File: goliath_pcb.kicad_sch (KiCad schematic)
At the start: 58 parts, among them IC1 MCT9001SD, IC2 MCT9001SD, IC3 MCT9001SD, IC4 MCT9001SD, IC5 MCT9001SD, IC6 MCT9001SD, IC7 MCT9001SD, J1 RJ45_LED, J2 RJ45_LED, J3 RJ45_LED, J4 RJ45_LED, J5 Conn_01x10, U1 Pico, U2 LM7805_TO220, U3 74HCT244, U4 74HCT244, U5 LTC1298CS8-PBF

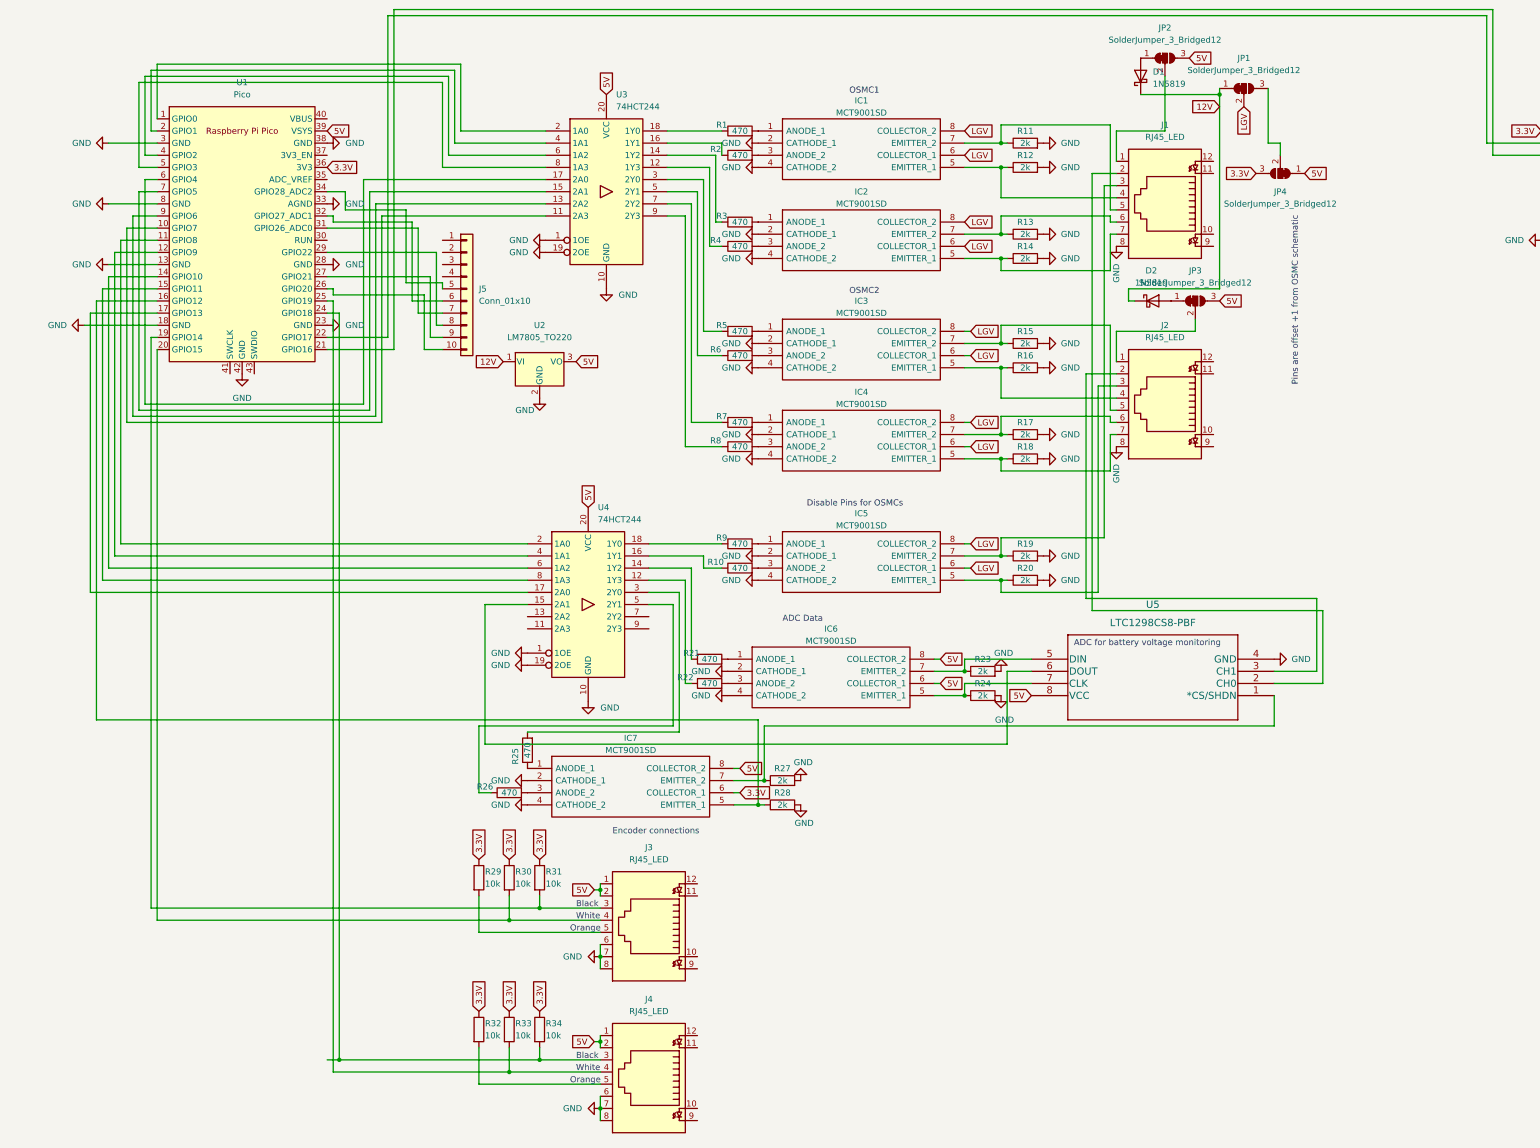
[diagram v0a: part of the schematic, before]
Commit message: Add extra I/O and extra headers, expand PCB
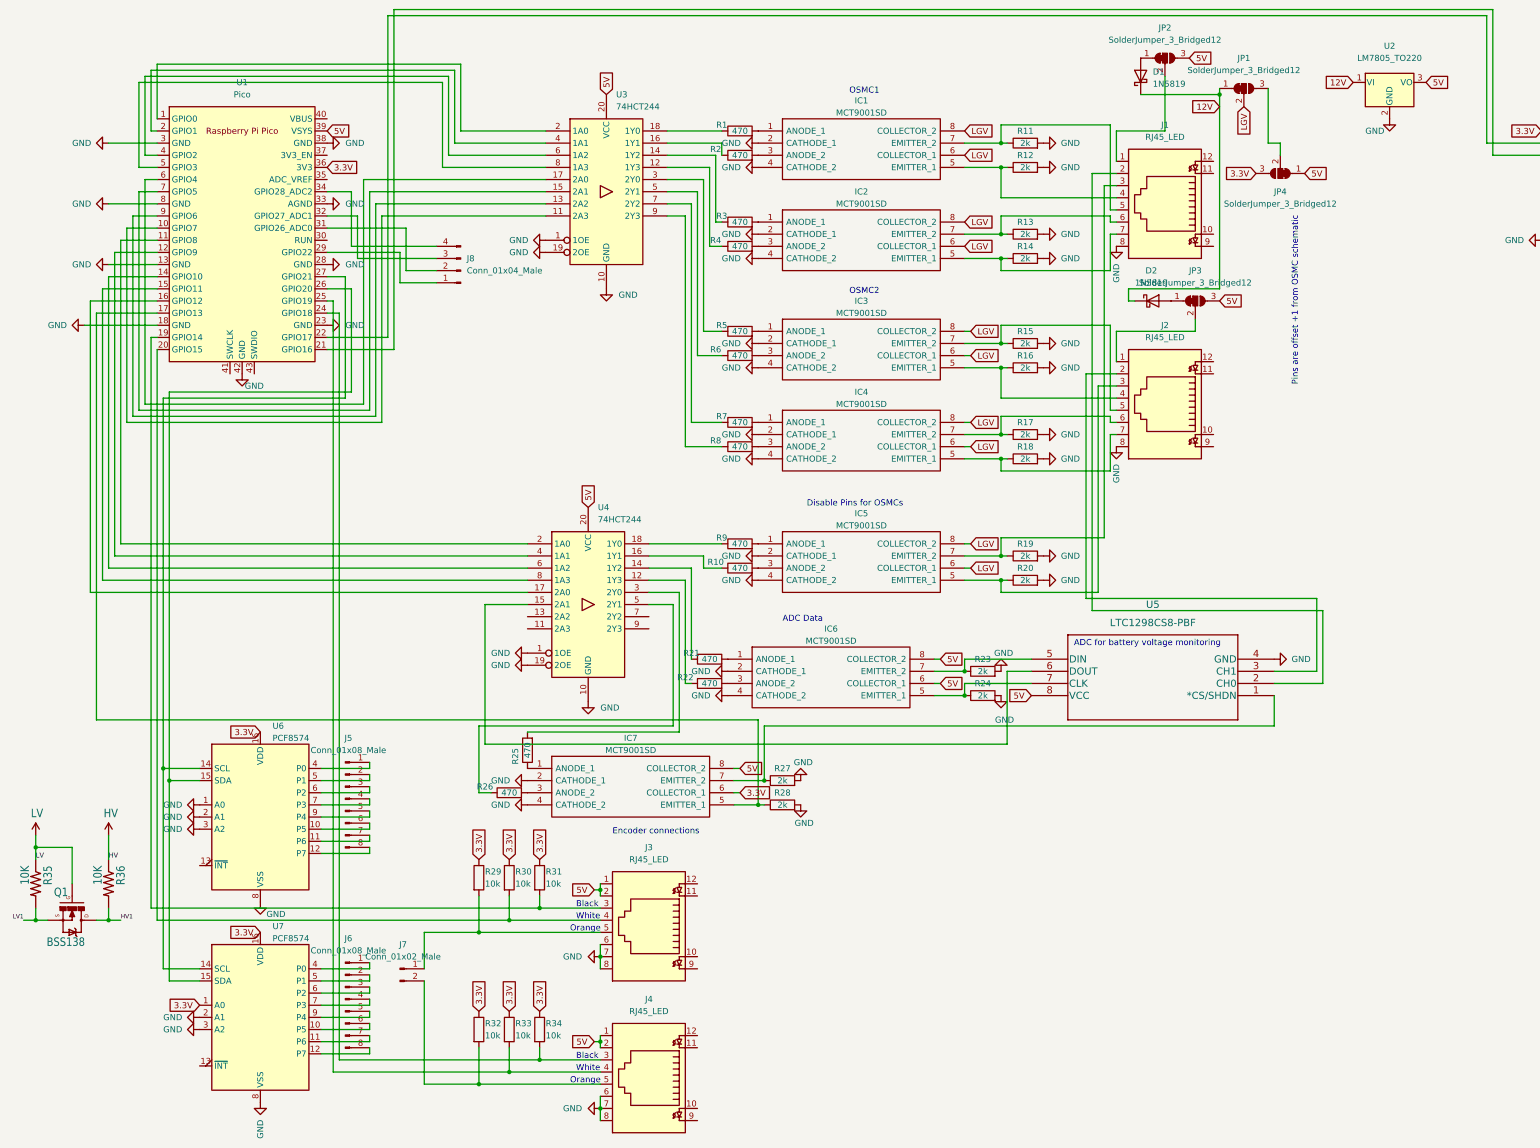
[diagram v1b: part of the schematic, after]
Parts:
- removed J5: Conn_01x10, symbol Connector_Generic:Conn_01x10
- added J5, J6: Conn_01x08_Male, Connector_PinHeader_2.54mm:PinHeader_1x08_P2.54mm_Vertical, symbol Connector:Conn_01x08_Male
- added J7: Conn_01x02_Male, Connector_PinHeader_2.54mm:PinHeader_1x02_P2.54mm_Vertical, symbol Connector:Conn_01x02_Male
- added J8: Conn_01x04_Male, Connector_PinHeader_2.54mm:PinHeader_1x04_P2.54mm_Vertical, symbol Connector:Conn_01x04_Male
- added Q1: BSS138, goliath_pcb:SOT23-3, symbol goliath_pcb-eagle-import:MOSFET-NCHANNELSMD
- added R35, R36: 10K, goliath_pcb:0603-RES, symbol goliath_pcb-eagle-import:RESISTOR0603-RES
- added U6, U7: PCF8574, Package_DIP:DIP-16_W7.62mm_Socket, symbol Interface_Expansion:PCF8574
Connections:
- net 3.3V: now also U6.16 (VDD), U7.1 (A0), U7.16 (VDD)
- net GND: now also U6.1 (A0), U6.2 (A1), U6.3 (A2), U6.8 (VSS), U7.2 (A1), U7.3 (A2), U7.8 (VSS)
- net at J3.5, R29.2: now also J7.1 (Pin_1)
- net at J4.5, R32.2: now also J7.2 (Pin_2)
- net at U4.17 (2A0): now also U1.16 (GPIO12); no longer U1.17 (GPIO13)
- net at IC7.5 (EMITTER_1), R28.1: now also U1.17 (GPIO13); no longer U1.16 (GPIO12)
- net at U1.26 (GPIO20): now also U6.15 (SDA), U7.15 (SDA)
- net at U1.27 (GPIO21): now also U6.14 (SCL), U7.14 (SCL)
- net at U1.29 (GPIO22): now also J8.1 (Pin_1)
- net at U1.31 (GPIO26_ADC0): now also J8.2 (Pin_2)
- net at U1.32 (GPIO27_ADC1): now also J8.3 (Pin_3)
- net at U1.34 (GPIO28_ADC2): now also J8.4 (Pin_4)
- new net: J6.6 (Pin_6), U7.10 (P5)
- new net: J6.7 (Pin_7), U7.11 (P6)
- new net: J6.8 (Pin_8), U7.12 (P7)
- new net: J6.1 (Pin_1), U7.4 (P0)
- new net: J6.2 (Pin_2), U7.5 (P1)
- new net: J6.3 (Pin_3), U7.6 (P2)
- new net: J6.4 (Pin_4), U7.7 (P3)
- new net: J6.5 (Pin_5), U7.9 (P4)
- new net: J5.1 (Pin_1), U6.4 (P0)
- new net: J5.2 (Pin_2), U6.5 (P1)
- new net: J5.3 (Pin_3), U6.6 (P2)
- new net: J5.4 (Pin_4), U6.7 (P3)
- new net: J5.5 (Pin_5), U6.9 (P4)
- new net: J5.6 (Pin_6), U6.10 (P5)
- new net: J5.7 (Pin_7), U6.11 (P6)
- new net: J5.8 (Pin_8), U6.12 (P7)
- new net HV1: Q1.3 (D), R36.2
- new net LV1: Q1.2 (S), R35.2
- new net VCC: Q1.1 (G), R35.1, R36.1
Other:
- moved on the sheet: U2

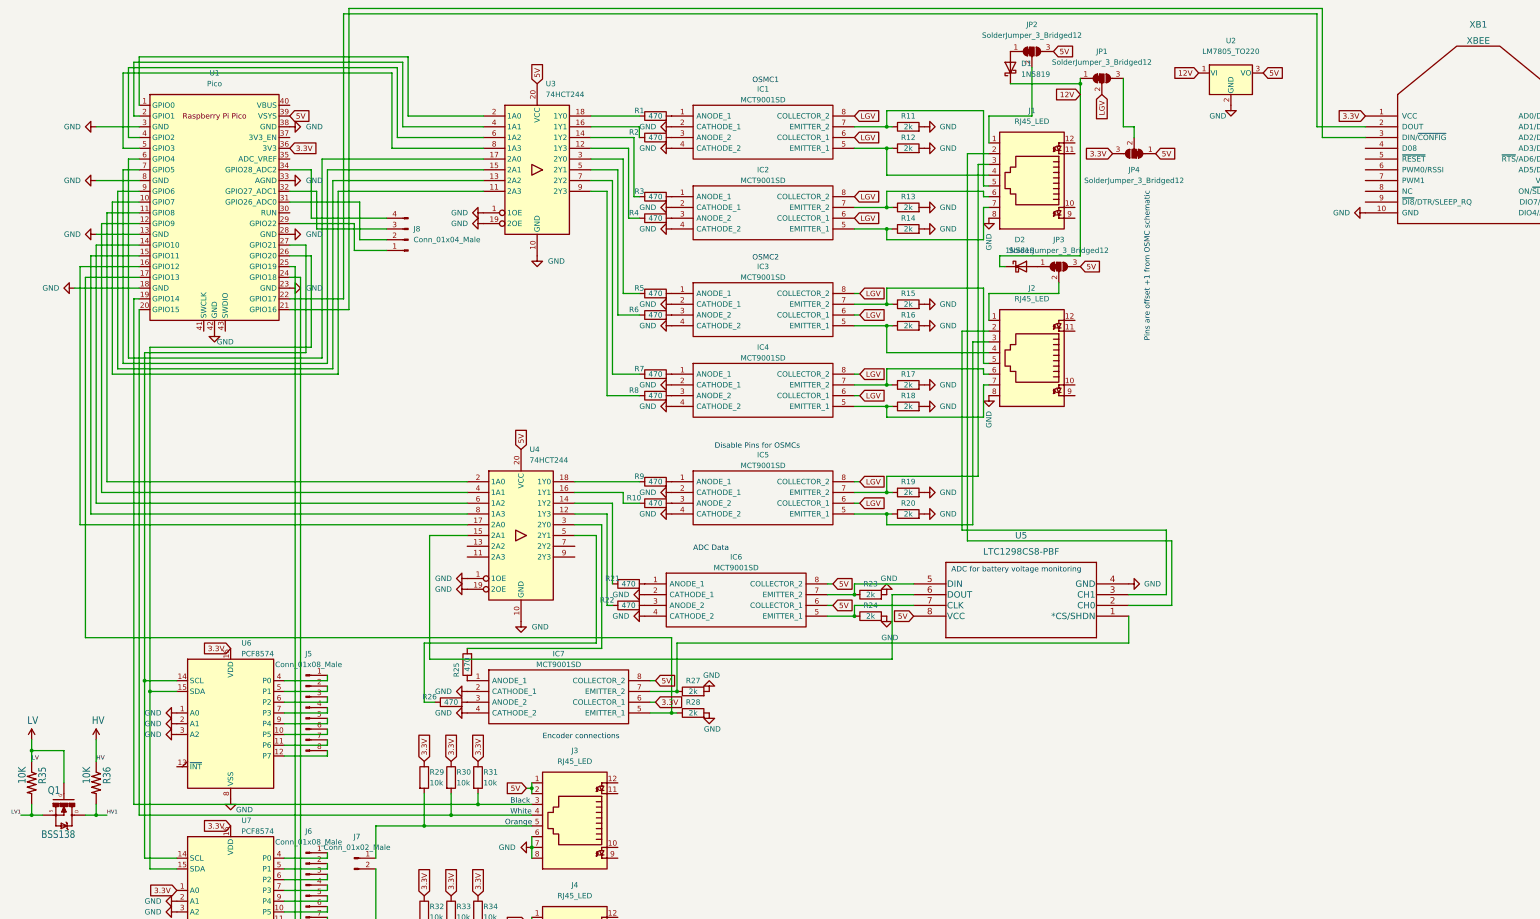
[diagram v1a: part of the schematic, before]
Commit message: Add more resistors, caps
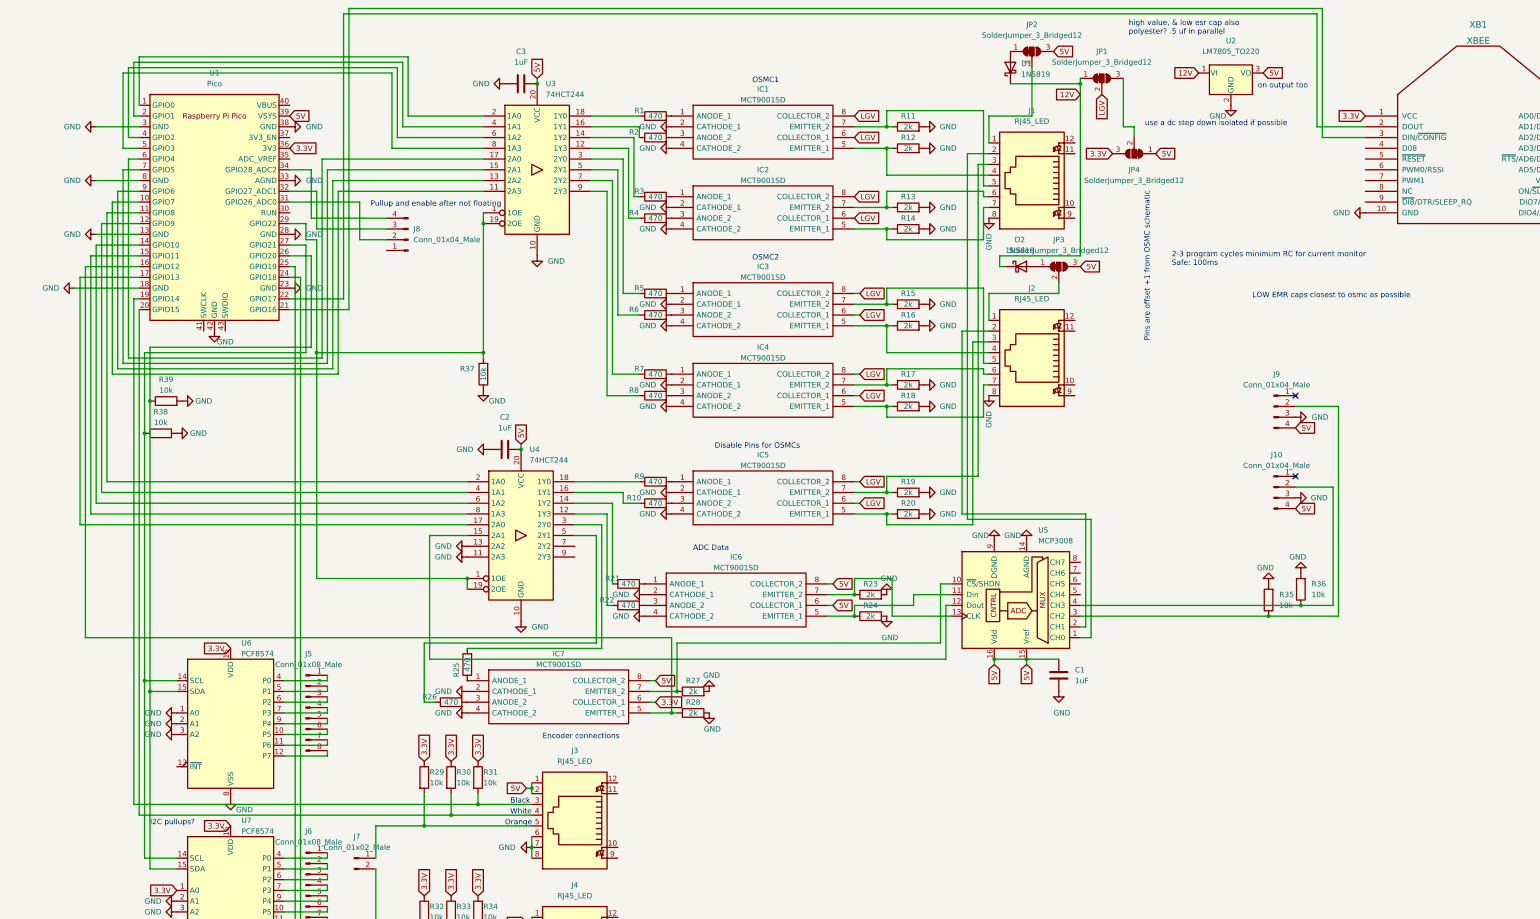
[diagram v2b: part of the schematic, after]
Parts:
- removed Q1: BSS138, goliath_pcb:SOT23-3, symbol goliath_pcb-eagle-import:MOSFET-NCHANNELSMD
- removed R35, R36: 10K, goliath_pcb:0603-RES, symbol goliath_pcb-eagle-import:RESISTOR0603-RES
- removed U5: LTC1298CS8-PBF, Package_DIP:DIP-8_W7.62mm_Socket, symbol LTC1298:LTC1298CS8-PBF
- added C1, C2, C3: 1uF, Capacitor_THT:C_Rect_L7.0mm_W4.5mm_P5.00mm, symbol Device:C
- added J10, J9: Conn_01x04_Male, Connector_PinHeader_2.54mm:PinHeader_1x04_P2.54mm_Vertical, symbol Connector:Conn_01x04_Male
- added R35, R36, R37, R38, R39: 10k, Resistor_THT:R_Axial_DIN0207_L6.3mm_D2.5mm_P10.16mm_Horizontal, symbol Device:R
- added U5: MCP3008, Package_DIP:DIP-16_W7.62mm_Socket, symbol Analog_ADC:MCP3008
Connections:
- net 5V: now also C1.1, C2.2, C3.2, J10.4 (Pin_4), J9.4 (Pin_4), U5.15 (Vref), U5.16 (Vdd)
- net GND: now also U4.11 (2A3), U4.13 (2A2), C1.2, C2.1, C3.1, J10.3 (Pin_3), J9.3 (Pin_3), R35.2, R36.2, R37.1, R38.2, R39.2, U5.14 (AGND), U5.9 (DGND); no longer U3.1 (1OE), U3.19 (2OE), U4.1 (1OE), U4.19 (2OE)
- net at IC6.5 (EMITTER_1), R24.1: now also U5.11 (Din)
- net at IC7.7 (EMITTER_2), R27.1: now also U5.10 (~{CS}/SHDN)
- net at J1.2: now also U5.1 (CH0)
- net at J2.2: now also U5.2 (CH1)
- net at IC6.7 (EMITTER_2), R23.1: now also U5.13 (CLK)
- net at U4.15 (2A1): now also U5.12 (Dout)
- net at U1.27 (GPIO21), U6.14 (SCL), U7.14 (SCL): now also R38.1
- net at U1.26 (GPIO20), U6.15 (SDA), U7.15 (SDA): now also R39.1
- net at U4.17 (2A0): now also U1.17 (GPIO13); no longer U1.16 (GPIO12)
- net at IC7.5 (EMITTER_1), R28.1: now also U1.16 (GPIO12); no longer U1.17 (GPIO13)
- net at U1.29 (GPIO22): now also U3.1 (1OE), U3.19 (2OE), U4.1 (1OE), U4.19 (2OE), R37.2; no longer J8.1 (Pin_1)
- new net: J9.2 (Pin_2), R35.1, U5.3 (CH2)
- new net: J10.2 (Pin_2), R36.1, U5.4 (CH3)
- no-connect marks 0 -> 2
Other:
- note added: "2-3 program cycles minimum RC for current monitor Safe: 100ms"
- note added: "I2C pullups?"
- note added: "LOW EMR caps closest to osmc as possible"
- note added: "Pullup and enable after not floating"
- note added: "high value, & low esr cap also polyester? .5 uf in parallel"
- note added: "on output too"
- note added: "use a dc step down isolated if possible"
- note removed: "ADC for battery voltage monitoring"

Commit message: Add mosfets and stuff
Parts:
- removed JP2, JP3: SolderJumper_3_Bridged12, Jumper:SolderJumper-3_P1.3mm_Open_Pad1.0x1.5mm, symbol Jumper:SolderJumper_3_Bridged12
- removed U2: LM7805_TO220, Package_TO_SOT_THT:TO-220-3_Vertical, symbol Regulator_Linear:LM7805_TO220
- added C4: 22uF, Capacitor_THT:C_Rect_L7.0mm_W4.5mm_P5.00mm, symbol Device:C_Polarized
- added C5: 13uF, Capacitor_THT:C_Rect_L7.0mm_W4.5mm_P5.00mm, symbol Device:C
- added C6, C7: 1uF, Capacitor_THT:C_Rect_L7.0mm_W4.5mm_P5.00mm, symbol Device:C
- added D2, D3, D5, D6, D7, D8: 1N5819, Diode_THT:D_DO-41_SOD81_P10.16mm_Horizontal, symbol Diode:1N5819
- added J11, J12, J13: Screw_Terminal_01x02, TerminalBlock_Phoenix:TerminalBlock_Phoenix_MKDS-1,5-2_1x02_P5.00mm_Horizontal, symbol Connector:Screw_Terminal_01x02
- added L1: 82uH, Inductor_THT:L_Axial_L6.6mm_D2.7mm_P10.16mm_Horizontal_Vishay_IM-2, symbol Device:L
- added Q1, Q2: STP2N80K5, STP2N80K5:STP2N80K5, symbol STP2N80K5:STP2N80K5
- added R40, R41: 33k, Resistor_THT:R_Axial_DIN0207_L6.3mm_D2.5mm_P10.16mm_Horizontal, symbol Device:R
- added R42, R43: 2k, Resistor_THT:R_Axial_DIN0207_L6.3mm_D2.5mm_P10.16mm_Horizontal, symbol Device:R
- added U2: LM2592HVT-5.0/NOPB, LM2592HVT:LM2592HVT-5.0&slash_NOPB, symbol LM2592HVT:LM2592HVT-3.3/NOPB
- C1: footprint Capacitor_THT:C_Rect_L7.0mm_W4.5mm_P5.00mm -> STP2N80K5:STP2N80K5
- renumbered D2 to D4, JP4 to JP2
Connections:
- net 5V: now also C5.1, L1.2, U2.4 (FB)
- net GND: now also C4.2, C5.2, C6.1, C7.1, D6.2 (A), J11.2 (Pin_2), Q1.3 (SOURCE), Q2.3 (SOURCE), R42.2, R43.2, U2.3 (GND), U2.5 (~{ON}/OFF)
- net at D4.2 (A): now also D3.1 (K)
- net at J2.1: now also D3.2 (A)
- net at J1.1: now also D1.2 (A)
- net at R35.1, U5.3 (CH2): now also C6.2, R40.2; no longer J9.2 (Pin_2)
- net at R36.1, U5.4 (CH3): now also C7.2, R41.2; no longer J10.2 (Pin_2)
- net at U4.7 (2Y2): now also Q1.1 (GATE), R42.1
- net at U4.9 (2Y3): now also Q2.1 (GATE), R43.1
- net 12V renamed VIN
- net VIN: now also C4.1, D2.1 (K), D7.1 (K), D8.1 (K), J11.1 (Pin_1), J12.1 (Pin_1), J13.1 (Pin_1), U2.1 (VIN); no longer D1.1 (K)
- new net: D8.2 (A), J13.2 (Pin_2), Q2.2 (DRAIN)
- new net: D5.1 (K), L1.1, U2.2 (OUTPUT)
- new net: D5.2 (A), D6.1 (K)
- new net: J9.2 (Pin_2), R40.1
- new net: D7.2 (A), J12.2 (Pin_2), Q1.2 (DRAIN)
- new net: J10.2 (Pin_2), R41.1
- new net: D1.1 (K), D2.2 (A)
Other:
- note added: "SRC"
- note removed: "2-3 program cycles minimum RC for current monitor Safe: 100ms"
- note removed: "I2C pullups?"
- note removed: "high value, & low esr cap also polyester? .5 uf in parallel"
- note removed: "on output too"
- note removed: "use a dc step down isolated if possible"
- moved on the sheet: D1, D4, R35

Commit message: Finish mosfet circuits, add grounding vias, mark at potential orderable prototype (add BOM)
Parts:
- C1: footprint STP2N80K5:STP2N80K5 -> Capacitor_THT:C_Rect_L7.0mm_W4.5mm_P5.00mm
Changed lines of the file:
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@@
       (effects (font (size 1.27 1.27)) (justify left))
     )
-    (property "Footprint" "STP2N80K5:STP2N80K5" (id 2) (at 254.9652 180.34 0)
+    (property "Footprint" "Capacitor_THT:C_Rect_L7.0mm_W4.5mm_P5.00mm" (id 2) (at 254.9652 180.34 0)
       (effects (font (size 1.27 1.27)) hide)
     )
@@
     )
     (path "/c16487bb-097e-43a5-931b-34a996e06ac6"
-      (reference "C1") (unit 1) (value "1uF") (footprint "STP2N80K5:STP2N80K5")
+      (reference "C1") (unit 1) (value "1uF") (footprint "Capacitor_THT:C_Rect_L7.0mm_W4.5mm_P5.00mm")
     )
     (path "/fe4ab8e8-5d62-441c-a62e-555fc182dff0"
